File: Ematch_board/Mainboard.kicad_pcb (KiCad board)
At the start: 4 copper layers, 57 x 53 mm, 127 parts, among them J1 Conn_01x02_Male, J10 Conn_01x02_Male, J11 Conn_Coaxial, J2 Conn_01x02_Male, J3 Conn_01x02_Male, J4 Conn_01x02_Male, J5 Conn_01x02_Male, J6 Conn_01x02_Male, J7 RBUS, J8 USB_C_Receptacle_USB2.0, J9 Conn_01x02_Male, Q1 MMDT2222A, Q51 PMV20ENR, Q52 PMV20ENR, Q53 PMV20ENR, Q54 PMV20ENR, Q55 PMV20ENR, Q56 PMV20ENR, U1 LTV-247, U2 LTC4411, U3 RT9025-25GSP, U4 LTC4411, U5 SN65HVD230, U6 CP2102-GMR-QFN28

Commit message: Added version numbering
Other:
- board text added: "FLINT & STEEL v1"
- board text removed: "FLINT & STEEL"
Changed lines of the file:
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@@
   (gr_rect (start 129.65 110.6) (end 139.65 120.6) (layer "B.SilkS") (width 0.12) (fill solid))
   (gr_line (start 118.159524 72.998417) (end 118.159524 118.98) (layer "Edge.Cuts") (width 0.05))
-  (gr_arc (start 121.65 122.474086) (mid 119.181782 121.449275) (end 118.159524 118.98) (layer "Edge.Cuts") (width 0.05))
+  (gr_arc (start 121.65 122.474086) (mid 119.181782 121.449276) (end 118.159524 118.98) (layer "Edge.Cuts") (width 0.05))
   (gr_arc (start 171.926045 69.474086) (mid 174.210985 70.417276) (end 175.159524 72.7) (layer "Edge.Cuts") (width 0.05))
   (gr_line (start 175.159524 119.04) (end 175.159524 72.7) (layer "Edge.Cuts") (width 0.05))
@@
   (gr_line (start 121.65 122.474086) (end 171.714009 122.474086) (layer "Edge.Cuts") (width 0.05))
   (gr_arc (start 118.159524 72.998417) (mid 119.178088 70.505661) (end 121.665488 69.474086) (layer "Edge.Cuts") (width 0.05))
-  (gr_text "FLINT & STEEL" (at 147.25 77.075) (layer "B.SilkS")
+  (gr_text "FLINT & STEEL v1" (at 145.767213 77.36846) (layer "B.SilkS")
     (effects (font (size 3.5 3.5) (thickness 0.6)) (justify mirror))
   )

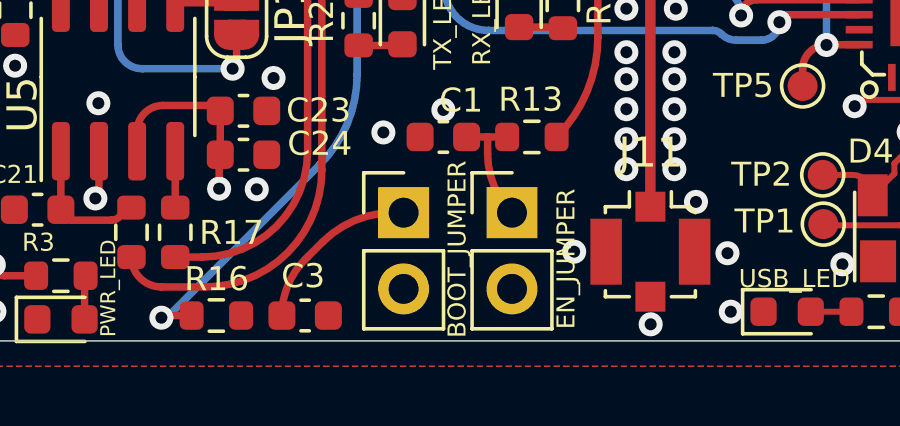
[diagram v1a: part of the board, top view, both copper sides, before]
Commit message: fixed unroute nets and changed LED resistor values
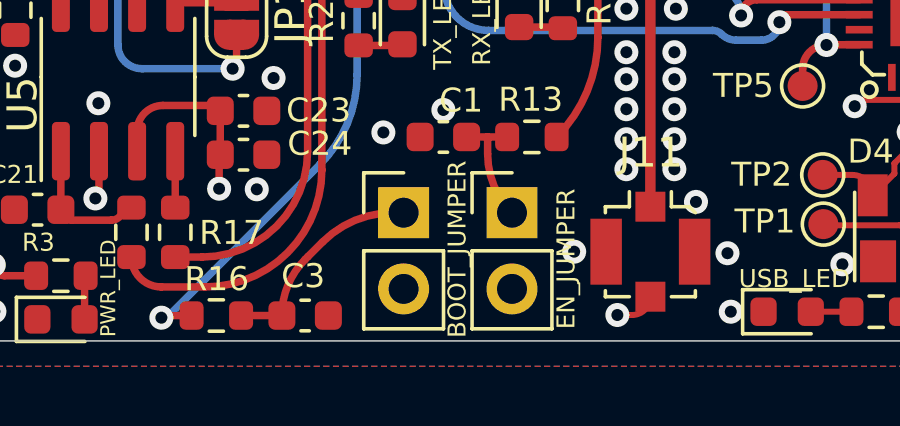
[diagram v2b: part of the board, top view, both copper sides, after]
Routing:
- net GND: track 31.9 -> 33.3 mm
- net Net-(C3-Pad1): track 5.83 -> 7.19 mm
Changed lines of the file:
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@@
   (segment (start 125.3625 120.5) (end 124.878553 120.5) (width 0.25) (layer "F.Cu") (net 7))
   (segment (start 151.85 95.05) (end 151.85 95.0288) (width 0.25) (layer "F.Cu") (net 7))
+  (segment (start 151.15 121.61) (end 151.64 121.61) (width 0.2) (layer "F.Cu") (net 7))
   (segment (start 133.870696 117.604304) (end 133.870696 116.15) (width 0.25) (layer "F.Cu") (net 7))
   (via (at 155.6 98.425) (size 0.8) (drill 0.4) (layers "F.Cu" "B.Cu") (free) (net 7))
@@
   (via (at 133.75 117.725) (size 0.8) (drill 0.4) (layers "F.Cu" "B.Cu") (free) (net 7))
   (via (at 129.95 118.125) (size 0.8) (drill 0.4) (layers "F.Cu" "B.Cu") (free) (net 7))
-  (via (at 152.26 121.92) (size 0.8) (drill 0.4) (layers "F.Cu" "B.Cu") (free) (net 7))
+  (via (at 151.15 121.61) (size 0.8) (drill 0.4) (layers "F.Cu" "B.Cu") (free) (net 7))
   (via (at 145.16 107.82) (size 0.8) (drill 0.4) (layers "F.Cu" "B.Cu") (net 7))
   (via (at 158.65 119.92) (size 0.8) (drill 0.4) (layers "F.Cu" "B.Cu") (free) (net 7))
@@
   (arc (start 151.295858 81.254142) (mid 151.311522 81.243676) (end 151.33 81.24) (width 0.25) (layer "F.Cu") (net 7))
   (arc (start 165.4196 118.0104) (mid 165.539803 117.720203) (end 165.83 117.6) (width 0.2) (layer "F.Cu") (net 7))
+  (arc (start 151.64 121.61) (mid 152.071335 121.431335) (end 152.25 121) (width 0.2) (layer "F.Cu") (net 7))
   (arc (start 133.75 117.725) (mid 133.835345 117.689649) (end 133.870696 117.604304) (width 0.25) (layer "F.Cu") (net 7))
   (arc (start 159.270489 114.439511) (mid 159.121651 114.501162) (end 159.06 114.65) (width 0.2) (layer "F.Cu") (net 7))
@@
   (segment (start 140.836259 119.663742) (end 141.325 119.175) (width 0.25) (layer "F.Cu") (net 51))
   (segment (start 140.740577 119.759424) (end 140.836259 119.663742) (width 0.25) (layer "F.Cu") (net 51))
+  (segment (start 139.966949 121.627127) (end 138.606949 121.627127) (width 0.25) (layer "F.Cu") (net 51))
   (segment (start 143.678858 118.2) (end 144.025 118.2) (width 0.25) (layer "F.Cu") (net 51))
   (arc (start 139.966949 121.627127) (mid 140.168008 120.616333) (end 140.740577 119.759424) (width 0.25) (layer "F.Cu") (net 51))

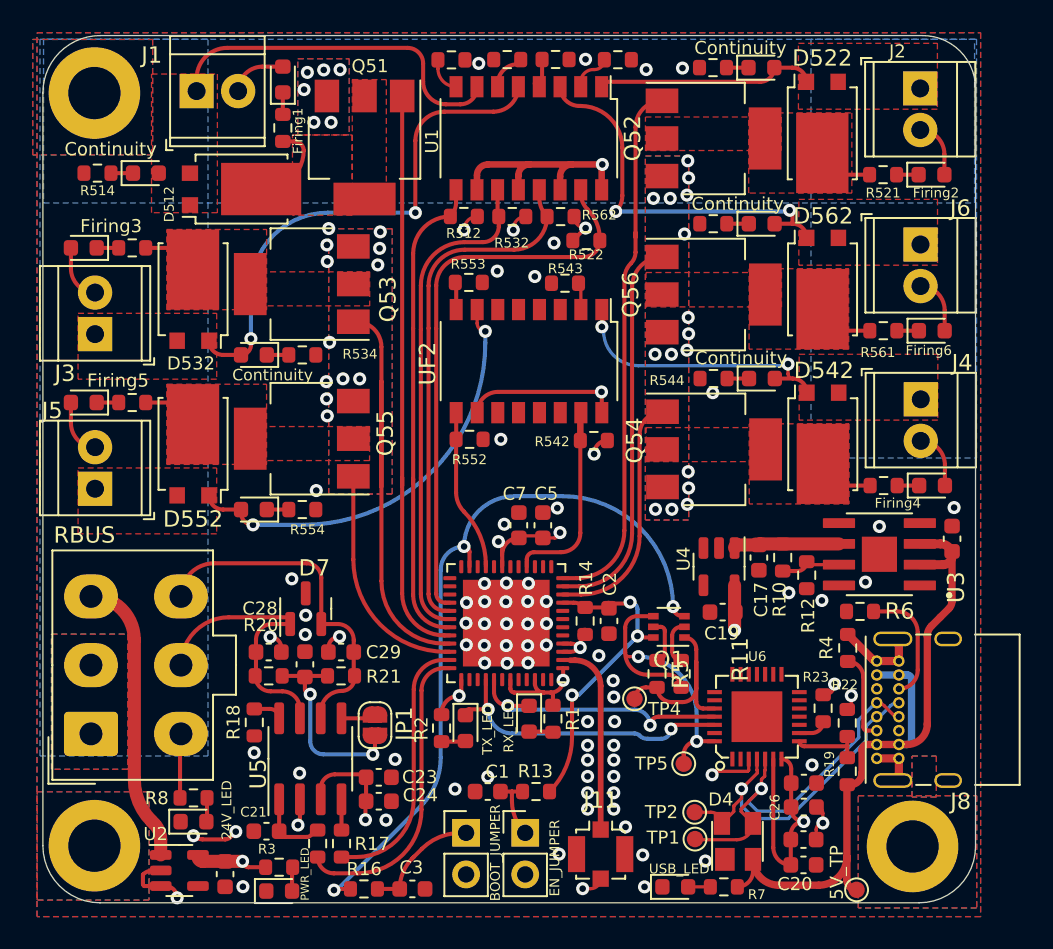
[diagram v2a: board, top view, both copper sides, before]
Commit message: moved nuke channels from input only pins, changed resistor values
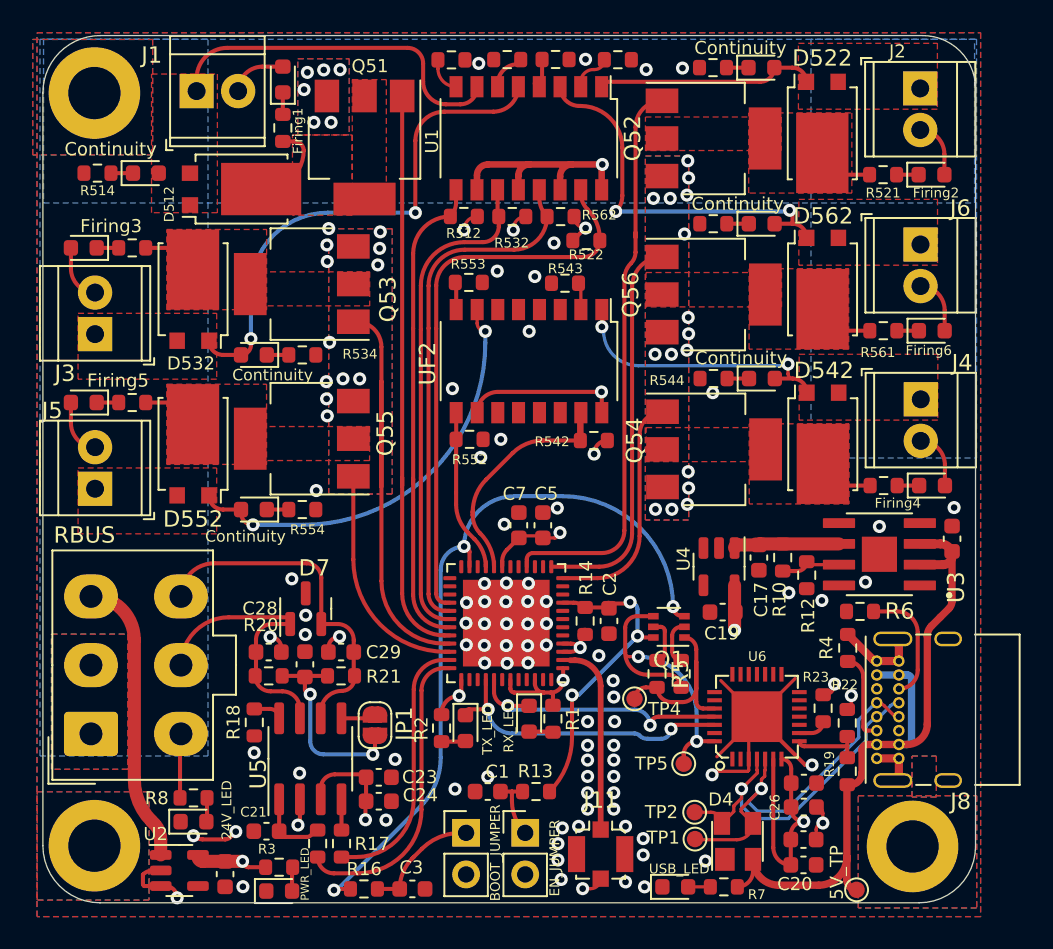
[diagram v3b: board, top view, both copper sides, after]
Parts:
- removed the G*** at (128.5, 94.3)
- C1, C3: value 1nF -> 0.1uF
- C27: value C -> 0.1uF
- C28, C29: value C_Small -> 220pF
- R20, R21: value R -> 60
- R511, R514, R521, R524, R531, R534, R541, R544, R551, R561, R564: value 1k -> 3k
- R8: value 3.5k -> 3k
- U3: value RT9025-25GSP -> SC4216H
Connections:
- GND1 pad 10: /Nuke 4 -> unconnected-(GND1-Pad10)
- GND1 pad 11: /Nuke 6 -> unconnected-(GND1-Pad11)
- GND1 pad 12: /Nuke 2 -> /Nuke 4
- GND1 pad 13: unconnected-(GND1-Pad13) -> /Nuke 6
- GND1 pad 16: /Cont 4 -> /Nuke 2
- GND1 pad 20: unconnected-(GND1-Pad20) -> /Cont 4
- U6 pad 29: unconnected-(U6-Pad29) -> GND
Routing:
- net GND: track 33.3 -> 50.7 mm, vias 117 -> 126
- net /Cont 4: track 11.9 -> 14.4 mm
- net /Nuke 2: track 32.9 -> 34.9 mm
- net +3V3: track 73.1 -> 72.0 mm, vias 12 -> 11
- net /Nuke 4: track 14.9 -> 14.4 mm

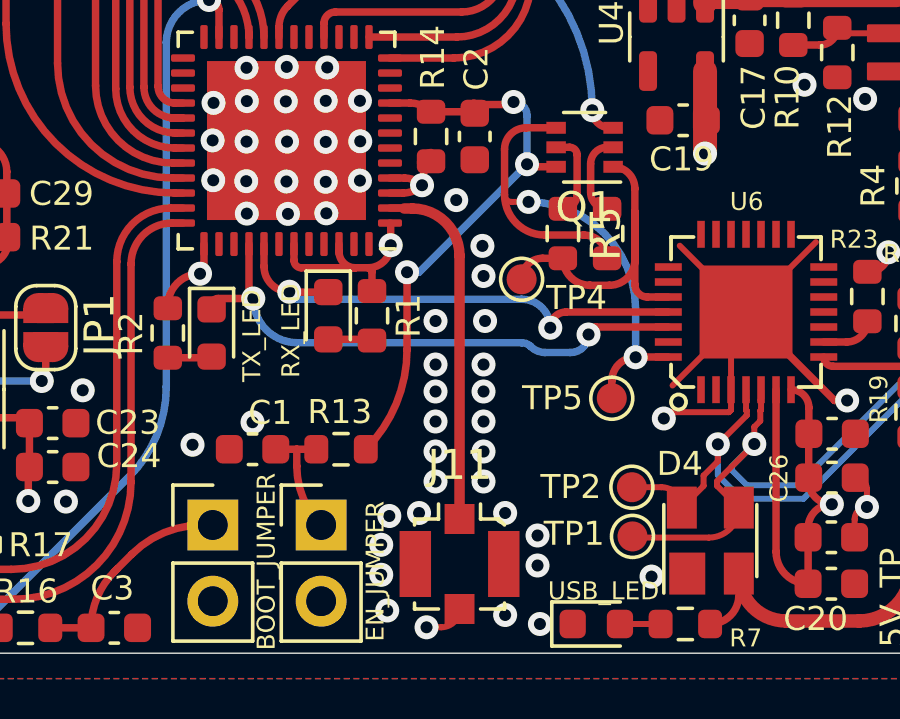
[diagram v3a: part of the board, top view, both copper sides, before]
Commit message: Added ICLR logo and fixed antenna line impedance
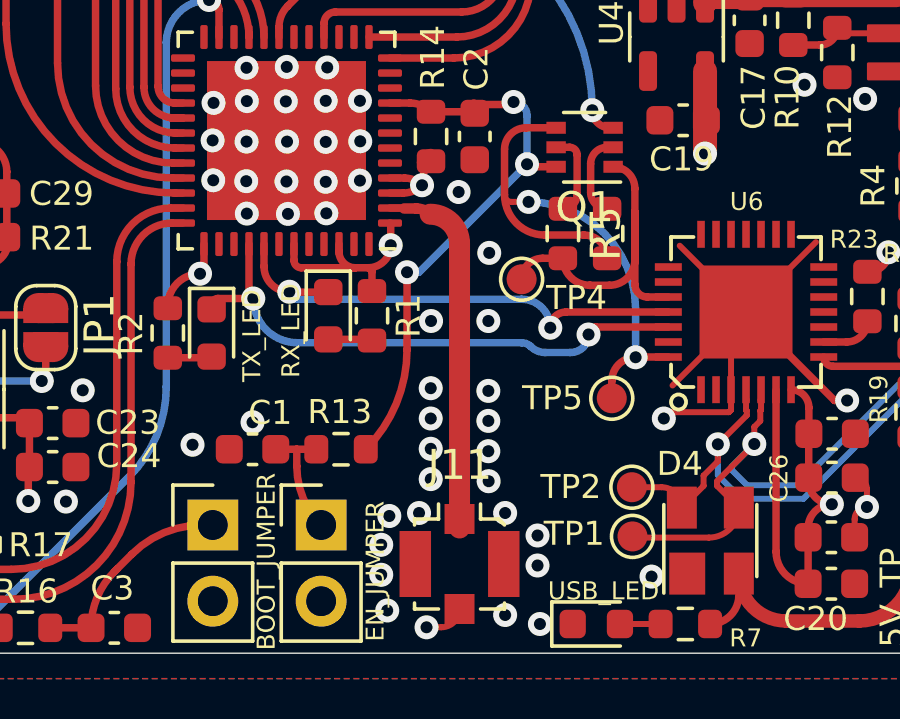
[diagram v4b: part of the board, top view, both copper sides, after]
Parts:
- added G***: LOGO, iclr:iclr_logo, B.Cu at (135.6, 91.0)
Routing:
- net GND: vias 126 -> 123

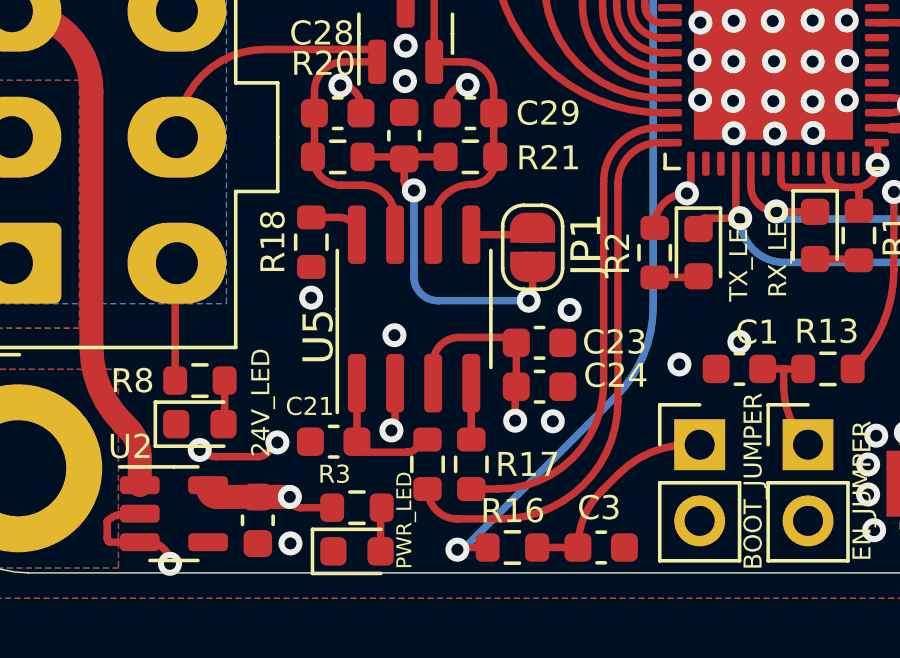
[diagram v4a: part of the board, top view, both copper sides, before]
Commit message: Removed CAN resistors
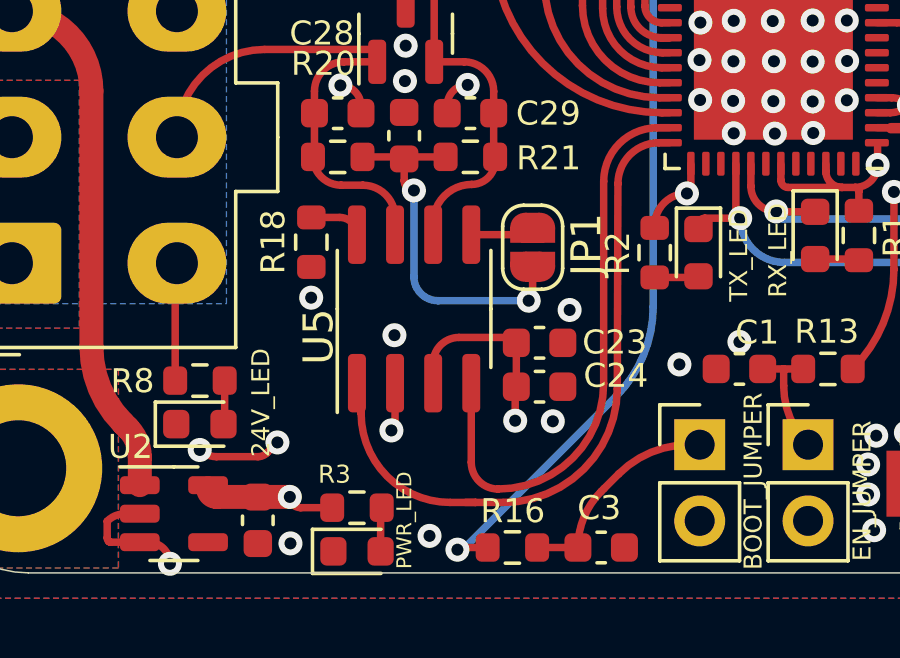
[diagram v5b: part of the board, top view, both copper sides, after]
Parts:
- removed C21: 160pF, Capacitor_SMD:C_0603_1608Metric
- removed R15, R17: 120, Resistor_SMD:R_0603_1608Metric
- C1, C2, C3: value 0.1uF -> 1uF
- R512, R513, R522, R523, R532, R533, R542, R543, R552, R553, R562, R563: value 500 -> 1k
- R554: value 1k -> 3k
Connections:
- U5 pad 1: Net-(C21-Pad2) -> /CAN_TX
- U5 pad 4: Net-(R17-Pad2) -> /CAN_RX
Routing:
- net Net-(C21-Pad2): track 4.78 -> 0.00 mm
- net /CAN_TX: track 18.7 -> 22.8 mm
- net /CAN_RX: track 16.2 -> 19.3 mm
- net Net-(R17-Pad2): track 1.88 -> 0.00 mm
- net GND: vias 123 -> 124

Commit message: DRC fixes
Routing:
- net /Nuke 3: track 29.5 -> 23.1 mm
- net /BOOT: track 45.8 -> 43.9 mm
- net Net-(D562-Pad1): track 23.8 -> 24.8 mm
- net Net-(C1-Pad1): track 4.84 -> 4.08 mm
- net /Vref: track 12.3 -> 11.6 mm
- net /Data+: track 21.9 -> 21.3 mm
- net Net-(R563-Pad1): track 2.05 -> 1.49 mm
